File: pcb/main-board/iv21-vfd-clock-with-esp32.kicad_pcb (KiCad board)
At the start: 2 copper layers, 101.5 x 40 mm, 29 parts, among them J1 Conn_02x10_Odd_Even, J2 4328, P1 USB_C_Plug_USB2.0, SW1 SW_SPST, SW2 SW_SPST, U1 MAX6921AQI_, U2 MOUDLE-SEEEDUINO-XIAO-ESP32C3, U3 AP3012, U4 S-1167B24

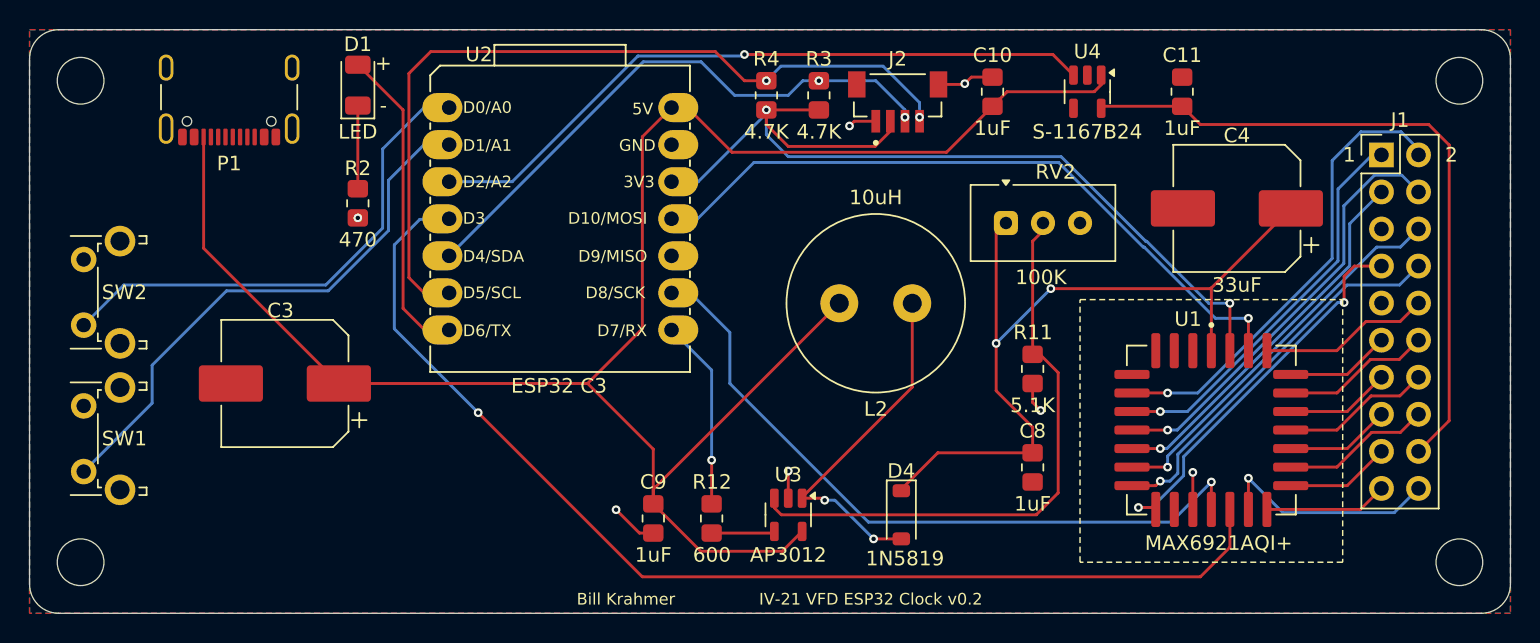
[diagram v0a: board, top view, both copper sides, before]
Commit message: Change inductor footprint.
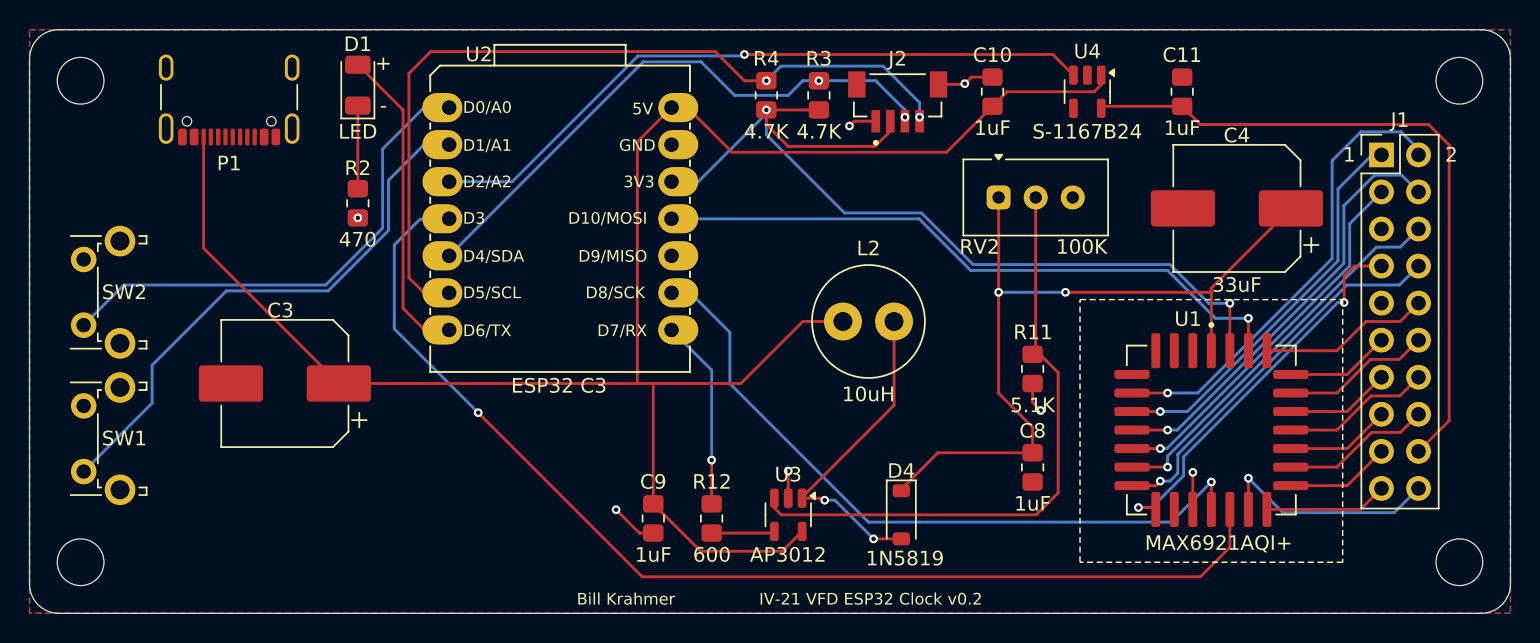
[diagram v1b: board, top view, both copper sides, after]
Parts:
- L2: footprint Inductor_THT:L_Radial_D12.0mm_P5.00mm_Fastron_11P -> Inductor_THT:L_Radial_D7.5mm_P3.50mm_Fastron_07P
- moved RV2 1.82 mm to (101.4, 29.5)
- moved L2 1.77 mm to (94.2, 38.0)
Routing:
- net Net-(U1-DIN): track 47.8 -> 44.6 mm
- net /5V: track 133.6 -> 130.6 mm
- net Net-(D4-A): track 24.4 -> 22.7 mm
- net Net-(U3-FB): track 40.7 -> 42.3 mm

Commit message: Some components PCB rearanging.
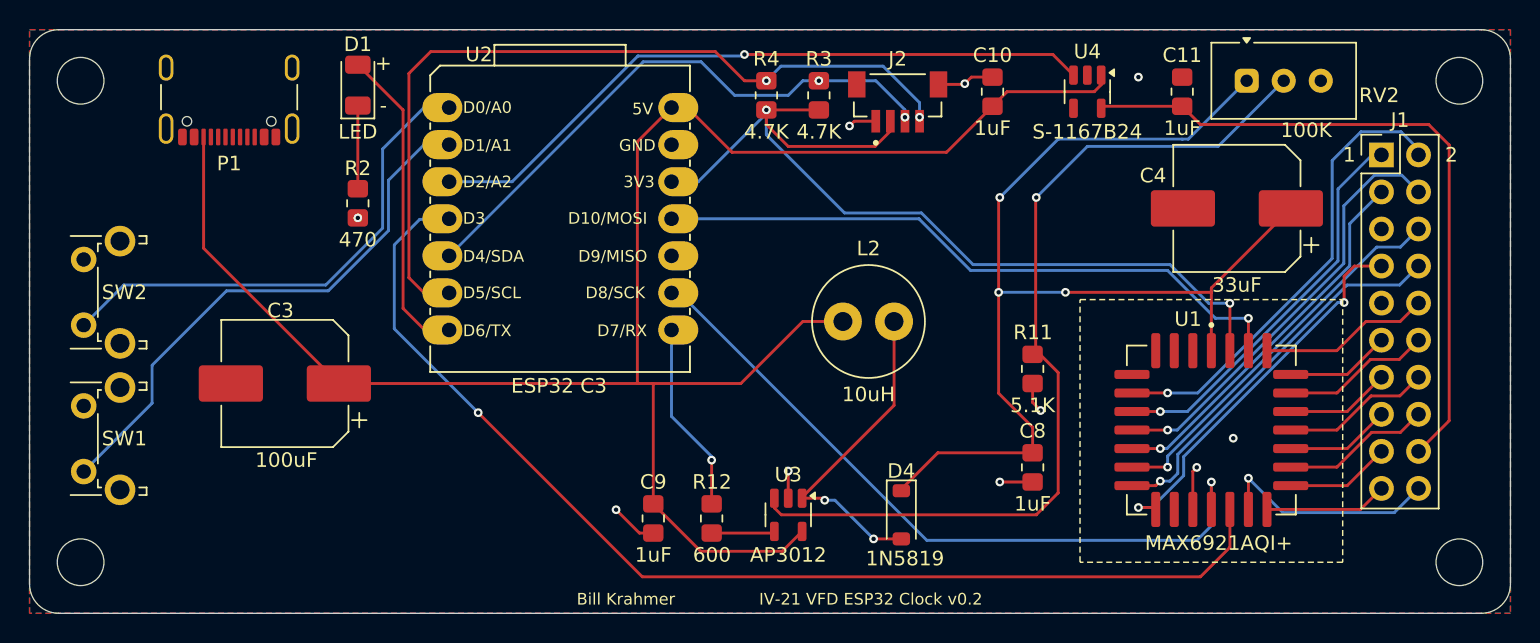
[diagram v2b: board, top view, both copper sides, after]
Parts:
- moved RV2 18.8 mm to (118.4, 21.5)
- moved G*** 9.30 mm to (62.0, 52.5)
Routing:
- net Net-(U3-FB): track 42.3 -> 62.6 mm, vias 0 -> 1
- net /VPP: track 55.2 -> 75.4 mm, vias 2 -> 3
- net GND: track 15.5 -> 18.2 mm, vias 7 -> 10
- net Net-(U1-CLK): track 48.6 -> 49.3 mm
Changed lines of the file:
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@@
 		(tags "capacitor electrolytic")
 		(property "Reference" "C4"
-			(at 0 5 0)
+			(at 5.75 2.25 0)
 			(layer "F.SilkS")
 			(effects
@@
 	(footprint "Potentiometer_THT:Potentiometer_Vishay_T93XA_Horizontal"
 		(layer "F.Cu")
-		(at 101.42 29.5)
+		(at 118.42 21.5)
 		(descr "Potentiometer, horizontal, Vishay, https://www.vishay.com/docs/51026/t93.pdf, 3/8\" x 3/8\" x 3/16\" (9.7 x 9.8 x 5mm max.)")
 		(tags "Potentiometer horizontal vishay")
 		(property "Reference" "RV2"
-			(at -1.31 3.3925 0)
+			(at 9.08 1 0)
 			(layer "F.SilkS")
 			(effects
@@
 		)
 		(property "Value" "100K"
-			(at 5.69 3.3925 0)
+			(at 4.08 3.3925 0)
 			(unlocked yes)
 			(layer "F.SilkS")
@@
 		)
 		(property "Value" "100uF"
-			(at -0.1 5.2 0)
-			(layer "F.Fab")
-			(hide yes)
+			(at -0.1 -5.25 0)
+			(layer "F.SilkS")
 			(effects
 				(font
@@
 	(footprint "wfk-logo:wfk-logo-8mmx8mm-f_mask"
 		(layer "F.Cu")
-		(at 52.75 53.5)
+		(at 62 52.5)
 		(property "Reference" "G***"
 			(at 0 0 0)
@@
 	)
 	(via
+		(at 101.5 29.5)
+		(size 0.6)
+		(drill 0.3)
+		(layers "F.Cu" "B.Cu")
+		(net 5)
+	)
+	(via
 		(at 101.42 36)
 		(size 0.6)
@@
 		(net 5)
 	)
+	(segment
+		(start 105.5 25.5)
+		(end 101.5 29.5)
+		(width 0.2)
+		(layer "B.Cu")
+		(net 5)
+	)
+	(segment
+		(start 114.42 25.5)
+		(end 114 25.5)
+		(width 0.2)
+		(layer "B.Cu")
+		(net 5)
+	)
+	(segment
+		(start 114 25.5)
+		(end 105.5 25.5)
+		(width 0.2)
+		(layer "B.Cu")
+		(net 5)
+	)
+	(segment
+		(start 118.42 21.5)
+		(end 114.42 25.5)
+		(width 0.2)
+		(layer "B.Cu")
+		(net 5)
+	)
 	(via
 		(at 95 24)
@@
 	)
 	(segment
-		(start 80.29 36.04)
-		(end 83 38.75)
+		(start 116 52)
+		(end 116 49)
 		(width 0.2)
 		(layer "B.Cu")
@@
 	)
 	(segment
-		(start 92.5 51.75)
-		(end 113.25 51.75)
+		(start 96.5 53)
+		(end 115 53)
 		(width 0.2)
 		(layer "B.Cu")
@@
 	(segment
 		(start 79 36.04)
-		(end 80.29 36.04)
+		(end 79.54 36.04)
 		(width 0.2)
 		(layer "B.Cu")
@@
 	)
 	(segment
-		(start 113.25 51.75)
-		(end 116 49)
+		(start 115 53)
+		(end 116 52)
 		(width 0.2)
 		(layer "B.Cu")
@@
 	)
 	(segment
-		(start 83 42.25)
-		(end 92.5 51.75)
-		(width 0.2)
-		(layer "B.Cu")
-		(net 35)
-	)
-	(segment
-		(start 83 38.75)
-		(end 83 42.25)
+		(start 79.54 36.04)
+		(end 96.5 53)
 		(width 0.2)
 		(layer "B.Cu")
@@
 	)
 	(segment
+		(start 115 48)
+		(end 114.729999 48.270001)
+		(width 0.2)
+		(layer "F.Cu")
+		(net 38)
+	)
+	(segment
 		(start 77.75 52.5)
 		(end 76.8 52.5)
@@
 	)
 	(segment
-		(start 114.729999 48.34)
-		(end 114.729999 50.88)
+		(start 76.8 52.5)
+		(end 75.2 50.9)
 		(width 0.2)
 		(layer "F.Cu")
@@
 	)
 	(segment
-		(start 76.8 52.5)
-		(end 75.2 50.9)
+		(start 114.729999 48.270001)
+		(end 114.729999 50.88)
 		(width 0.2)
 		(layer "F.Cu")
@@
 	)
 	(segment
+		(start 103.75 49)
+		(end 101.5 49)
+		(width 0.2)
+		(layer "F.Cu")
+		(net 38)
+	)
+	(segment
 		(start 101 21.25)
 		(end 99.55 21.25)
@@
 	)
 	(via
+		(at 101.5 49)
+		(size 0.6)
+		(drill 0.3)
+		(layers "F.Cu" "B.Cu")
+		(net 38)
+	)
+	(via
 		(at 91.2 24.6)
 		(size 0.6)
@@
 	)
 	(via
+		(at 111 21.25)
+		(size 0.6)
+		(drill 0.3)
+		(layers "F.Cu" "B.Cu")
+		(net 38)
+	)
+	(via
+		(at 117.5 46)
+		(size 0.6)
+		(drill 0.3)
+		(layers "F.Cu" "B.Cu")
+		(free yes)
+		(net 38)
+	)
+	(via
 		(at 99.1 21.7)
 		(size 0.6)
@@
 	)
 	(via
-		(at 114.729999 48.34)
+		(at 115 48)
 		(size 0.6)
 		(drill 0.3)
@@
 	)
 	(segment
-		(start 81.75 41.33)
+		(start 79 44.5)
+		(end 81.75 47.25)
+		(width 0.2)
+		(layer "B.Cu")
+		(net 40)
+	)
+	(segment
+		(start 81.75 47.25)
 		(end 81.75 47.5)
 		(width 0.2)
@@
 	(segment
 		(start 79 38.58)
-		(end 81.75 41.33)
+		(end 79 44.5)
 		(width 0.2)
 		(layer "B.Cu")
@@
 		(net 54)
 	)
+	(via
+		(at 104 29.5)
+		(size 0.6)
+		(drill 0.3)
+		(layers "F.Cu" "B.Cu")
+		(net 54)
+	)
+	(segment
+		(start 120.96 21.5)
+		(end 116.46 26)
+		(width 0.2)
+		(layer "B.Cu")
+		(net 54)
+	)
+	(segment
+		(start 116.46 26)
+		(end 107.5 26)
+		(width 0.2)
+		(layer "B.Cu")
+		(net 54)
+	)
+	(segment
+		(start 107.5 26)
+		(end 104 29.5)
+		(width 0.2)
+		(layer "B.Cu")
+		(net 54)
+	)
 	(zone
 		(net 0)
@@
 		(min_thickness 0.25)
 		(filled_areas_thickness no)
-		(fill
+		(fill yes
 			(thermal_gap 0.5)
 			(thermal_bridge_width 0.5)

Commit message: Add voltage regulator schematic symbol from dad.
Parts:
- moved U4 0.12 mm to (107.5, 22.1)

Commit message: Add some grounding vias.
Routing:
- net GND: vias 10 -> 12
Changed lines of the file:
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@@
+	)
+	(via
+		(at 43.5 37.5)
+		(size 0.6)
+		(drill 0.3)
+		(layers "F.Cu" "B.Cu")
+		(net 38)
+	)
+	(via
+		(at 85 28.5)
+		(size 0.6)
+		(drill 0.3)
+		(layers "F.Cu" "B.Cu")
+		(free yes)
+		(net 38)
 	)
 	(via
